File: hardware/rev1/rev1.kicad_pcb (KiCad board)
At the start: 2 copper layers, 83.8 x 86.7 mm, 37 parts, among them J1 Conn_01x09_Female, J2 RFM9X_header, J3 Conn_01x03_Male, U1 BNO055, U2 MPL3115A2, U3 Teensy3.6, U4 BMI088, U5 ADXL345BCCZ, Y1 Crystal_32kHz768

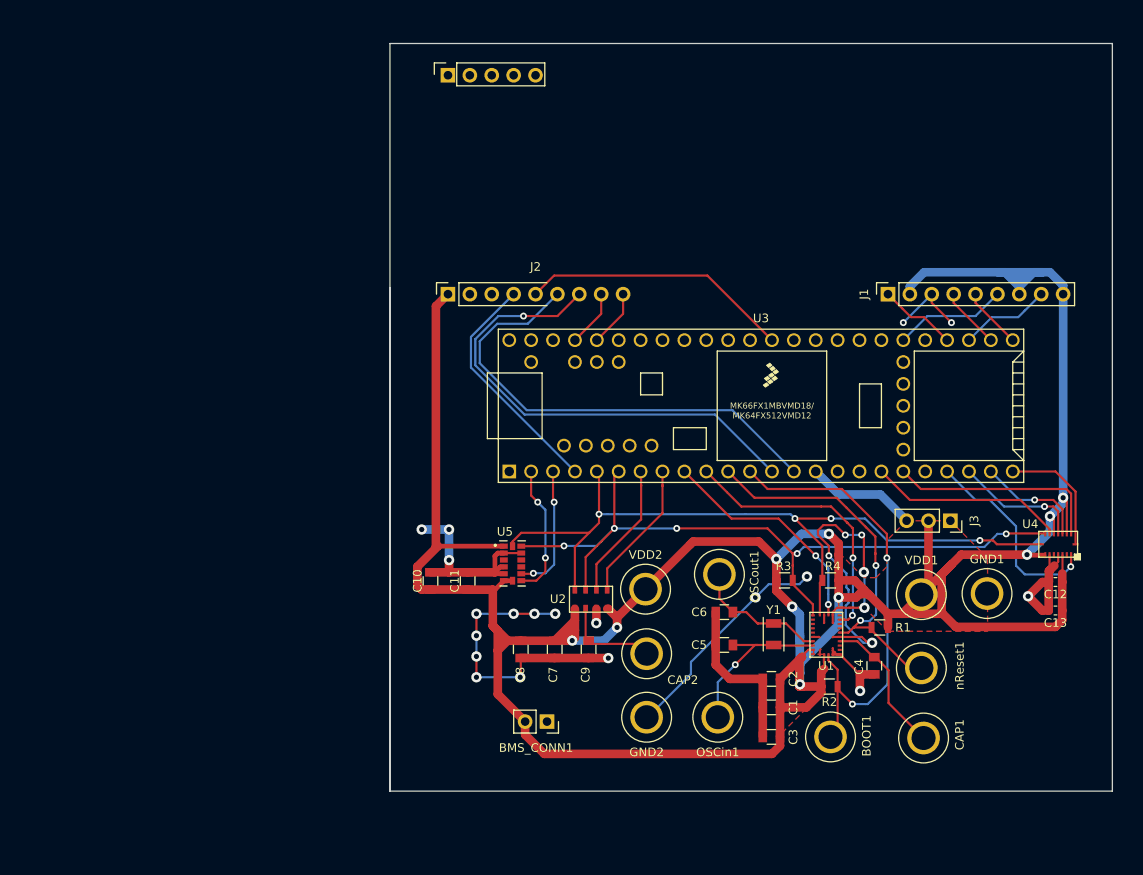
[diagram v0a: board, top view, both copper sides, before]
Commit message: add diode between Vin on Teensy and VDD on BMS
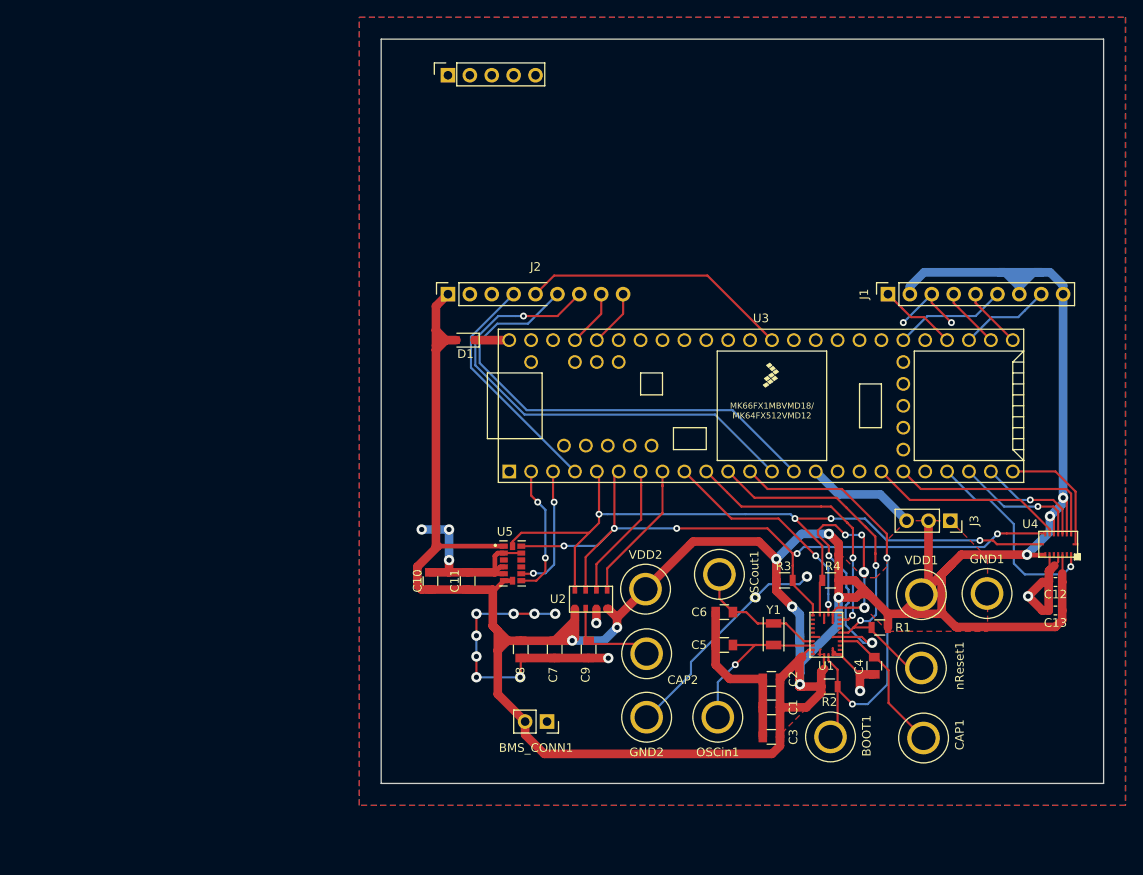
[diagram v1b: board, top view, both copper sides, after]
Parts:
- added D1: D, footprints:D_0805_OEM, F.Cu at (110.4, 87.4)
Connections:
- U3 pad 53: Net-(U3-Pad53) -> VIN_5V
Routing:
- net 3.3VBMS: track 377.5 -> 381.9 mm
- net VIN_5V: track 0.00 -> 4.03 mm
- added copper zone on B.Cu, net GND
- added copper zone on F.Cu, net GND
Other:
- board size 83.8 x 86.7 mm -> 83.8 x 86.4 mm

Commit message: add olin logo and design information
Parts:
- added G***: , footprints:OLIN_O, F.Cu at (174.6, 58.2)
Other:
- board text added: "Olin Rocketry Rev 1 1/24/2021 Ian Eykamp"
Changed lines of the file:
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@@
   (general
     (thickness 1.6)
-    (drawings 4)
+    (drawings 5)
     (tracks 594)
     (zones 0)
-    (modules 38)
+    (modules 39)
     (nets 83)
   )
@@
     )
   )
+  (module footprints:OLIN_O (layer F.Cu)
+    (at 174.625 58.166)
+    (tags "Olin O logo")
+    (fp_text reference G*** (at 5.08 -5.08) (layer F.SilkS) hide
+      (effects (font (size 1.524 1.524) (thickness 0.3)))
+    )
+    (fp_text value "" (at 5.08 -7.62) (layer F.SilkS) hide
+      (effects (font (size 1.524 1.524) (thickness 0.3)))
+    )
+    (fp_poly (pts (xy 3.442983 -3.189143) (xy 3.593457 -3.149129) (xy 3.859628 -3.080824) (xy 4.192829 -2.996675)
+      (xy 4.318 -2.965353) (xy 4.950523 -2.771412) (xy 5.589166 -2.511366) (xy 6.187709 -2.208074)
+      (xy 6.699928 -1.884399) (xy 7.006464 -1.635631) (xy 7.427728 -1.15255) (xy 7.68721 -0.655705)
+      (xy 7.791208 -0.151883) (xy 7.746021 0.352128) (xy 7.557949 0.849541) (xy 7.23329 1.333569)
+      (xy 6.778343 1.797426) (xy 6.199408 2.234324) (xy 5.502783 2.637476) (xy 4.694767 3.000096)
+      (xy 3.78166 3.315395) (xy 2.769759 3.576588) (xy 2.037525 3.718298) (xy 1.579989 3.791873)
+      (xy 1.263227 3.832252) (xy 1.062288 3.841026) (xy 0.952225 3.819783) (xy 0.916988 3.789688)
+      (xy 0.858074 3.735928) (xy 0.847963 3.779733) (xy 0.766319 3.839404) (xy 0.537525 3.878973)
+      (xy 0.3175 3.891838) (xy -0.049381 3.903054) (xy -0.420533 3.915266) (xy -0.613858 3.922106)
+      (xy -0.848176 3.919314) (xy -0.993137 3.895498) (xy -1.016025 3.876157) (xy -1.081706 3.846379)
+      (xy -1.164166 3.861997) (xy -1.171663 3.848862) (xy -1.054877 3.771153) (xy -0.838402 3.644985)
+      (xy -0.801282 3.624227) (xy -0.008948 3.11414) (xy 0.773964 2.467576) (xy 1.356472 1.894766)
+      (xy 2.033545 1.129263) (xy 2.578075 0.383663) (xy 3.016751 -0.379744) (xy 3.126149 -0.605915)
+      (xy 3.414204 -1.311966) (xy 3.572957 -1.91735) (xy 3.603305 -2.429665) (xy 3.50615 -2.856508)
+      (xy 3.413505 -3.034819) (xy 3.334494 -3.173405) (xy 3.358577 -3.208225) (xy 3.442983 -3.189143)) (layer F.SilkS) (width 0.01))
+    (fp_poly (pts (xy 0.78907 -2.933726) (xy 0.297169 -2.603291) (xy -0.249654 -2.169905) (xy -0.811 -1.670573)
+      (xy -1.346471 -1.1423) (xy -1.815667 -0.622091) (xy -2.036037 -0.345931) (xy -2.493304 0.320664)
+      (xy -2.866143 0.986545) (xy -3.148527 1.632052) (xy -3.33443 2.237523) (xy -3.417825 2.783297)
+      (xy -3.392687 3.249711) (xy -3.252989 3.617104) (xy -3.251451 3.6195) (xy -3.169272 3.757194)
+      (xy -3.151881 3.805837) (xy -3.238357 3.784085) (xy -3.451232 3.729169) (xy -3.753084 3.650766)
+      (xy -3.937 3.602827) (xy -4.929803 3.301284) (xy -5.762117 2.955854) (xy -6.437575 2.564339)
+      (xy -6.959808 2.124543) (xy -7.332449 1.634266) (xy -7.40086 1.507176) (xy -7.582592 0.976433)
+      (xy -7.604253 0.451032) (xy -7.475103 -0.063274) (xy -7.204403 -0.560731) (xy -6.801416 -1.035585)
+      (xy -6.275401 -1.482082) (xy -5.63562 -1.894469) (xy -4.891334 -2.266991) (xy -4.051805 -2.593894)
+      (xy -3.126293 -2.869426) (xy -2.12406 -3.087831) (xy -1.054367 -3.243355) (xy 0.073526 -3.330246)
+      (xy 0.403482 -3.341618) (xy 1.526631 -3.369785) (xy 0.78907 -2.933726)) (layer F.SilkS) (width 0.01))
+  )
+  (gr_text "Olin Rocketry\nRev 1\n1/24/2021\nIan Eykamp" (at 174.244 66.167) (layer F.SilkS)
+    (effects (font (size 1 1) (thickness 0.15)))
+  )
   (gr_line (start 184.404 138.811) (end 100.584 138.811) (angle 90) (layer Edge.Cuts) (width 0.05))

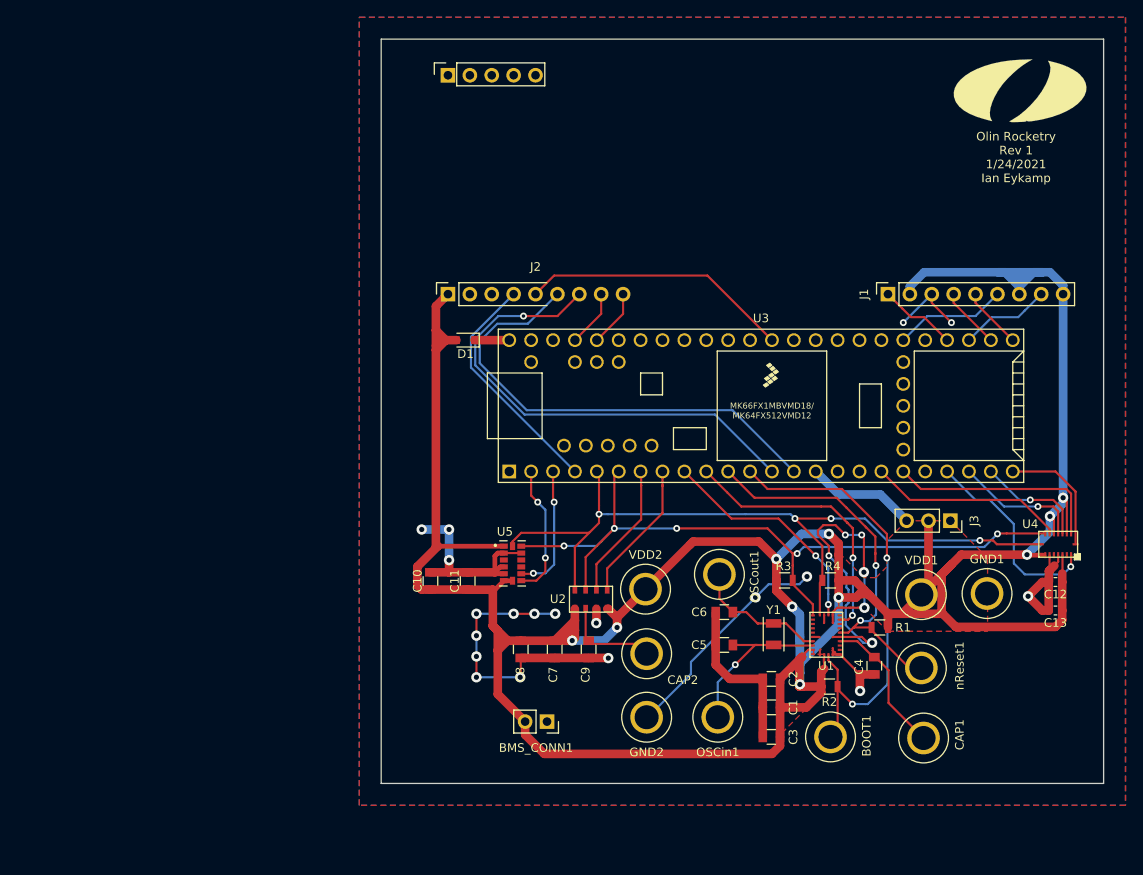
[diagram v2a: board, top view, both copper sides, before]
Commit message: move GPS pins away from Teensy
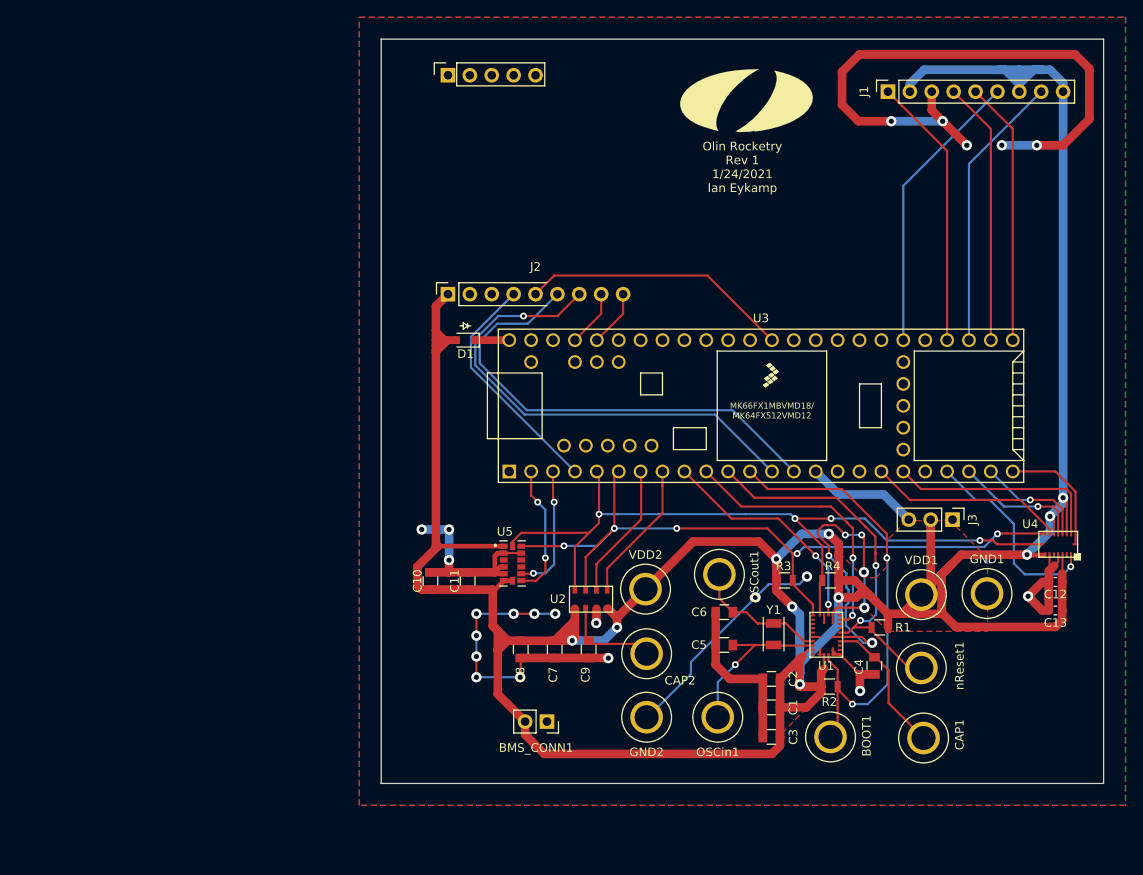
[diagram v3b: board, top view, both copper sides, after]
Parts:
- J3: footprint Connector_PinSocket_2.54mm:PinSocket_1x03_P2.54mm_Vertical -> Connector_PinHeader_2.54mm:PinHeader_1x03_P2.54mm_Vertical
- moved G*** 31.8 mm to (142.9, 59.3)
- moved J1 23.5 mm to (159.4, 58.5)
- moved J3 0.28 mm to (166.9, 108.2)
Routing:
- net GND: track 182.6 -> 245.4 mm, vias 25 -> 28
- net 3.3VBMS: track 381.9 -> 409.1 mm
- net TX: track 7.12 -> 30.6 mm
- net RX: track 7.12 -> 30.6 mm
- net PPS: track 9.07 -> 31.7 mm
- net ENABLE_GPS: track 10.6 -> 32.3 mm
- net FIX: track 13.1 -> 33.4 mm
- removed copper zone on F.Cu, net VDD

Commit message: wip
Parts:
- removed G***: , footprints:OLIN_O
- added D2: D, footprints:D_0805_OEM, F.Cu at (89.0, 143.0)
- added D3: D, footprints:D_0805_OEM, F.Cu at (75.4, 143.0)
- added Q1: Q_PNP_BCE, Package_TO_SOT_THT:TO-220-3_Horizontal_TabDown, F.Cu at (65.8, 138.6)
- added R5: R_1.07K, footprints:R_0805_OEM, F.Cu at (85.2, 130.4)
- BMS_CONN1: value Conn_01x02_Male -> Conn_01x04_Male; footprint Connector_PinHeader_2.54mm:PinHeader_1x02_P2.54mm_Vertical -> Connector_PinHeader_2.54mm:PinHeader_1x04_P2.54mm_Vertical
- moved D1 52.6 mm to (80.1, 130.4), turned to 270 degrees
- moved BMS_CONN1 32.7 mm to (87.8, 138.0), turned to 270 degrees
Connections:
- net VIN_5V renamed BMS_to_Teensy
- BMS_CONN1 pad 2: 3.3VBMS -> BMS_to_sensors
- C1 pad 1: 3.3VBMS -> +3V3
- C10 pad 1: 3.3VBMS -> +3V3
- C11 pad 1: 3.3VBMS -> +3V3
- C12 pad 1: 3.3VBMS -> +3V3
- C13 pad 1: 3.3VBMS -> +3V3
- C2 pad 2: 3.3VBMS -> +3V3
- C3 pad 2: 3.3VBMS -> +3V3
- C7 pad 1: 3.3VBMS -> +3V3
- C8 pad 1: 3.3VBMS -> +3V3
- D1 pad 2: 3.3VBMS -> Net-(BMS_CONN1-Pad4)
- J1 pad 2: 3.3VBMS -> +3V3
- J1 pad 7: 3.3VBMS -> Net-(J1-Pad7)
- J1 pad 9: 3.3VBMS -> Net-(J1-Pad9)
- J2 pad 9: 3.3VBMS -> +3V3
- J3 pad 2: 3.3VBMS -> +3V3
- R1 pad 1: 3.3VBMS -> +3V3
- R2 pad 1: 3.3VBMS -> +3V3
- R3 pad 1: 3.3VBMS -> +3V3
- R4 pad 1: 3.3VBMS -> +3V3
- U1 pad 28: 3.3VBMS -> +3V3
- U1 pad 3: 3.3VBMS -> +3V3
- U2 pad 1: 3.3VBMS -> +3V3
- U2 pad 4: 3.3VBMS -> +3V3
- U3 pad 30: TX -> RX
- U3 pad 31: RX -> TX
- U4 pad 11: 3.3VBMS -> +3V3
- U4 pad 14: 3.3VBMS -> +3V3
- U4 pad 3: 3.3VBMS -> +3V3
- U4 pad 7: 3.3VBMS -> +3V3
- U5 pad 1: 3.3VBMS -> +3V3
- U5 pad 6: 3.3VBMS -> +3V3
- U5 pad 7: 3.3VBMS -> +3V3
- VDD1 pad 1: 3.3VBMS -> +3V3
- VDD2 pad 1: 3.3VBMS -> +3V3
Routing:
- net BMS_to_sensors_backup: track 0.00 -> 14.1 mm
- net Net-(D3-Pad2): track 0.00 -> 7.85 mm
- net BMS_to_sensors: track 0.00 -> 6.10 mm
- net +3V3: track 0.00 -> 1.13 mm
- net 3.3VBMS: track 409.1 -> 408.0 mm
- added copper zone on F.Cu, net +3V3
- removed copper zone on F.Cu, net 3.3VBMS

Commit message: wip
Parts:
- added BMS_CONN2: Conn_01x04_Male, Connector_PinHeader_2.54mm:PinHeader_1x04_P2.54mm_Vertical, F.Cu at (82.9, 136.0)
- moved D1 8.87 mm to (71.4, 131.8)
- moved R5 7.58 mm to (77.9, 132.2), turned to 0 degrees
- moved BMS_CONN1 5.14 mm to (82.9, 139.8)
- moved D2 5.14 mm to (84.2, 144.8)
- moved D3 5.14 mm to (70.6, 144.8)
- moved Q1 5.14 mm to (61.0, 140.4)
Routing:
- net 3.3VBMS: track 408.0 -> 360.9 mm
- net GND: track 245.4 -> 225.3 mm, vias 28 -> 20
- net Net-(Q1-Pad1): track 0.00 -> 19.4 mm, vias 0 -> 1
- net +3V3: track 1.13 -> 17.0 mm
- net Net-(BMS_CONN1-Pad4): track 0.00 -> 9.92 mm
- net BMS_to_sensors: track 6.10 -> 14.4 mm
- net BMS_to_Teensy: track 4.03 -> 0.00 mm
- net BMS_to_sensors_backup: track 14.1 -> 17.9 mm

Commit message: wip
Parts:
- moved D1 43.1 mm to (114.4, 129.7)
- moved D2 43.1 mm to (127.3, 142.6)
- moved D3 43.1 mm to (113.7, 142.6)
- moved BMS_CONN1 43.1 mm to (126.0, 137.7)
- moved BMS_CONN2 43.1 mm to (126.0, 133.9)
- moved Q1 43.1 mm to (104.0, 138.2)
- moved R5 43.1 mm to (120.9, 130.0)
- moved GND2 1.79 mm to (133.0, 130.3)
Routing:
- net BMS_to_Teensy: track 0.00 -> 44.6 mm, vias 0 -> 2
- net GND: track 225.3 -> 223.9 mm

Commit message: wip
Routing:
- net 3.3VBMS: track 360.9 -> 385.5 mm
- net TX: track 30.6 -> 6.11 mm
- net RX: track 30.6 -> 6.11 mm
- net SCL_TEENSY: track 90.1 -> 90.6 mm
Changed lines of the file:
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@@
     (thickness 1.6)
     (drawings 11)
-    (tracks 628)
+    (tracks 630)
     (zones 0)
     (modules 43)
@@
   )
   (setup
-    (last_trace_width 0.9)
+    (last_trace_width 0.25)
     (user_trace_width 0.475)
     (user_trace_width 0.55)
@@
   (segment (start 151.4799 119.2484) (end 151.4799 115.5401) (width 0.25) (layer F.Cu) (net 9) (status C00030))
   (segment (start 151.4799 115.5401) (end 151.7675 115.2525) (width 0.25) (layer F.Cu) (net 9) (status 30))
-  (segment (start 123.0549 116.3119) (end 123.0549 111.379) (width 0.25) (layer F.Cu) (net 9) (status 400010))
-  (segment (start 123.0549 111.379) (end 123.0549 111.3871) (width 0.25) (layer F.Cu) (net 9))
-  (segment (start 123.0549 111.379) (end 123.063 111.379) (width 0.25) (layer F.Cu) (net 9))
-  (segment (start 123.063 111.379) (end 124.714 109.728) (width 0.25) (layer F.Cu) (net 9))
-  (segment (start 124.714 109.728) (end 125.857 108.585) (width 0.25) (layer F.Cu) (net 9))
+  (segment (start 123.0549 116.3119) (end 123.0549 111.887) (width 0.25) (layer F.Cu) (net 9) (status 400010))
+  (segment (start 125.857 109.0849) (end 125.222 109.7199) (width 0.25) (layer F.Cu) (net 9))
+  (segment (start 125.222 109.7199) (end 123.0549 111.887) (width 0.25) (layer F.Cu) (net 9))
+  (segment (start 125.857 108.585) (end 125.857 109.0849) (width 0.25) (layer F.Cu) (net 9))
   (segment (start 125.857 108.585) (end 125.857 107.569) (width 0.25) (layer F.Cu) (net 9))
   (segment (start 125.857 107.569) (end 125.857 106.553) (width 0.25) (layer F.Cu) (net 9))
@@
   (via (at 148.59 108.077) (size 0.8) (drill 0.4) (layers F.Cu B.Cu) (net 9))
   (segment (start 115.824 111.274) (end 115.824 110.744) (width 0.25) (layer F.Cu) (net 9) (status 400010))
-  (segment (start 116.84 109.728) (end 124.714 109.728) (width 0.25) (layer F.Cu) (net 9))
+  (segment (start 125.222 109.728) (end 125.222 109.7199) (width 0.25) (layer F.Cu) (net 9))
+  (segment (start 125.2139 109.728) (end 125.222 109.728) (width 0.25) (layer F.Cu) (net 9))
+  (segment (start 116.84 109.728) (end 125.2139 109.728) (width 0.25) (layer F.Cu) (net 9))
   (segment (start 115.824 110.744) (end 116.84 109.728) (width 0.25) (layer F.Cu) (net 9))
   (segment (start 128.016 107.569) (end 126.873 107.569) (width 0.25) (layer B.Cu) (net 9))
@@
   (segment (start 181.1485 104.9485) (end 178.816 102.616) (width 0.25) (layer F.Cu) (net 55))
   (segment (start 169.545 58.547) (end 169.545 58.547) (width 0.25) (layer F.Cu) (net 56) (status C00010))
-  (segment (start 173.863 62.865) (end 173.863 87.376) (width 0.25) (layer F.Cu) (net 56) (status 800000))
   (segment (start 169.545 58.547) (end 173.863 62.865) (width 0.25) (layer F.Cu) (net 56) (status 400020))
   (segment (start 167.005 58.547) (end 167.005 58.547) (width 0.25) (layer F.Cu) (net 57) (status C00010))
-  (segment (start 171.323 62.865) (end 171.323 87.376) (width 0.25) (layer F.Cu) (net 57) (status 800000))
   (segment (start 167.005 58.547) (end 171.323 62.865) (width 0.25) (layer F.Cu) (net 57) (status 400020))
   (segment (start 177.165 58.547) (end 175.26 60.452) (width 0.25) (layer B.Cu) (net 58) (status 400010))
@@
   (segment (start 116.7765 122.2535) (end 115.316 122.2535) (width 1) (layer F.Cu) (net 78) (status 400010))
   (segment (start 115.316 122.2535) (end 115.2365 122.2535) (width 1) (layer F.Cu) (net 78))
-  (segment (start 115.2365 122.2535) (end 114.1095 123.3805) (width 1) (layer F.Cu) (net 78))
+  (segment (start 128.905 130.556) (end 128.905 139.954) (width 1) (layer F.Cu) (net 78))
+  (segment (start 125.476 127.127) (end 128.905 130.556) (width 1) (layer F.Cu) (net 78))
+  (segment (start 116.84 127.127) (end 125.476 127.127) (width 1) (layer F.Cu) (net 78))
+  (segment (start 115.2365 125.5235) (end 116.84 127.127) (width 1) (layer F.Cu) (net 78))
+  (segment (start 115.2365 122.2535) (end 115.2365 125.5235) (width 1) (layer F.Cu) (net 78))
   (via (at 146.4335 112.7785) (size 1.2) (drill 0.6) (layers F.Cu B.Cu) (net 78))
   (segment (start 146.4335 112.7785) (end 149.357 109.855) (width 1) (layer B.Cu) (net 78))
@@
   (segment (start 113.538 116.332) (end 113.538 120.523) (width 1) (layer F.Cu) (net 78))
   (segment (start 113.538 120.523) (end 113.538 120.555) (width 1) (layer F.Cu) (net 78))
-  (segment (start 114.1095 123.3805) (end 114.1095 121.0945) (width 1) (layer F.Cu) (net 78))
   (segment (start 114.1095 121.0945) (end 113.538 120.523) (width 1) (layer F.Cu) (net 78))
   (segment (start 115.316 122.2535) (end 115.2685 122.2535) (width 1) (layer F.Cu) (net 78))

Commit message: fix netlist, wip
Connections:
- C1 pad 1: +3V3 -> 3.3VBMS
- C10 pad 1: +3V3 -> 3.3VBMS
- C11 pad 1: +3V3 -> 3.3VBMS
- C12 pad 1: +3V3 -> 3.3VBMS
- C13 pad 1: +3V3 -> 3.3VBMS
- C2 pad 2: +3V3 -> 3.3VBMS
- C3 pad 2: +3V3 -> 3.3VBMS
- C7 pad 1: +3V3 -> 3.3VBMS
- C8 pad 1: +3V3 -> 3.3VBMS
- D2 pad 1: +3V3 -> 3.3VBMS
- D3 pad 1: +3V3 -> 3.3VBMS
- J1 pad 2: +3V3 -> 3.3VBMS
- J2 pad 9: +3V3 -> 3.3VBMS
- J3 pad 2: +3V3 -> 3.3VBMS
- R1 pad 1: +3V3 -> 3.3VBMS
- R2 pad 1: +3V3 -> 3.3VBMS
- R3 pad 1: +3V3 -> 3.3VBMS
- R4 pad 1: +3V3 -> 3.3VBMS
- U1 pad 28: +3V3 -> 3.3VBMS
- U1 pad 3: +3V3 -> 3.3VBMS
- U2 pad 1: +3V3 -> 3.3VBMS
- U2 pad 4: +3V3 -> 3.3VBMS
- U4 pad 11: +3V3 -> 3.3VBMS
- U4 pad 14: +3V3 -> 3.3VBMS
- U4 pad 3: +3V3 -> 3.3VBMS
- U4 pad 7: +3V3 -> 3.3VBMS
- U5 pad 1: +3V3 -> 3.3VBMS
- U5 pad 6: +3V3 -> 3.3VBMS
- U5 pad 7: +3V3 -> 3.3VBMS
- VDD1 pad 1: +3V3 -> 3.3VBMS
- VDD2 pad 1: +3V3 -> 3.3VBMS
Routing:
- net +3V3: track 17.0 -> 0.00 mm
- net 3.3VBMS: track 385.5 -> 402.5 mm
